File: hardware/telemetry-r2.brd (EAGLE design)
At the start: 65 x 56 mm, 96 parts, among them IC1 RA02, IC10 TPS70933, IC2 TPS70933, IC3 BME280, IC4 STM32L052C8T6, IC5 TPS62160, IC6 HX1, IC7 LMP7702, IC8 ADXL345, IC9 VN5160S-E, J1 GPS1, J2 RASPBERRYPI-GPIO, J3 POWER, J4 GPS2, J5 DNP, J6 SMA_EDGE, Y1 32768, Y2 8M

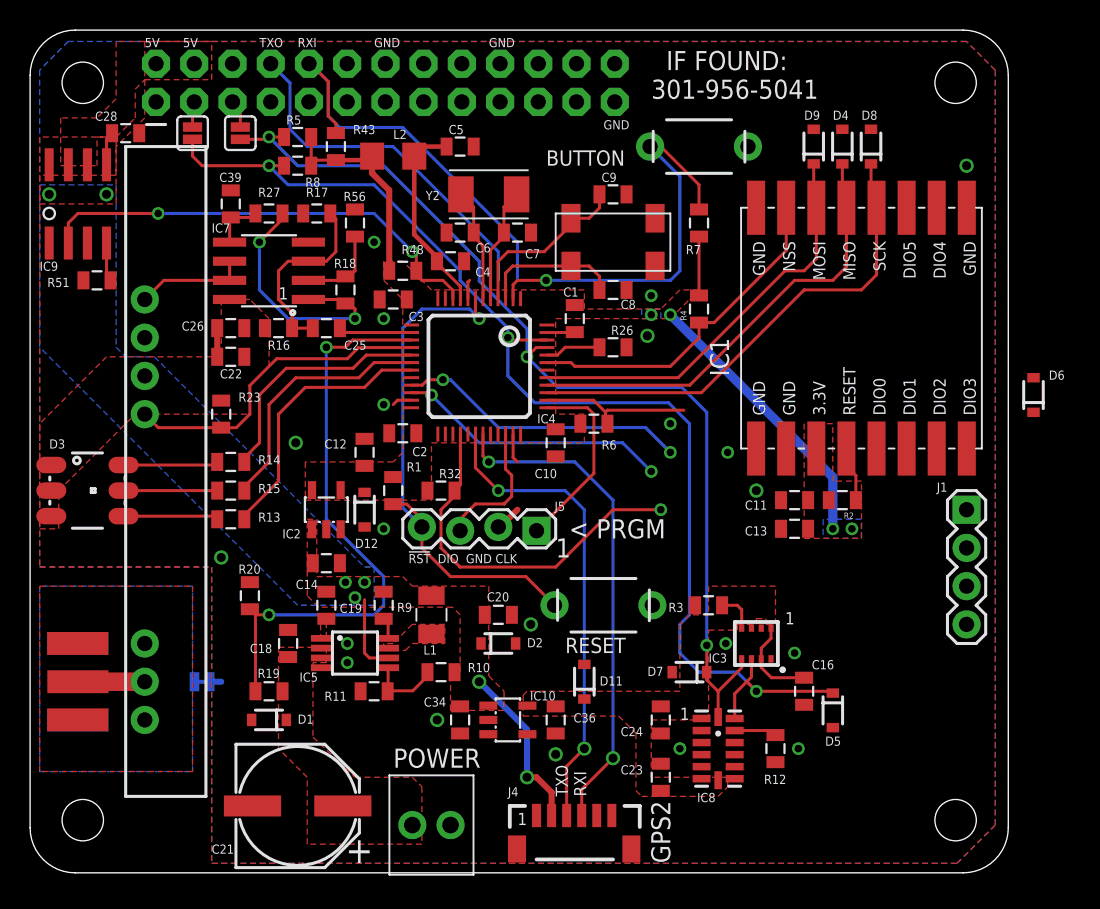
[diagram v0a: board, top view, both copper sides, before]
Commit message: Initial route for HAB v3 modular base board
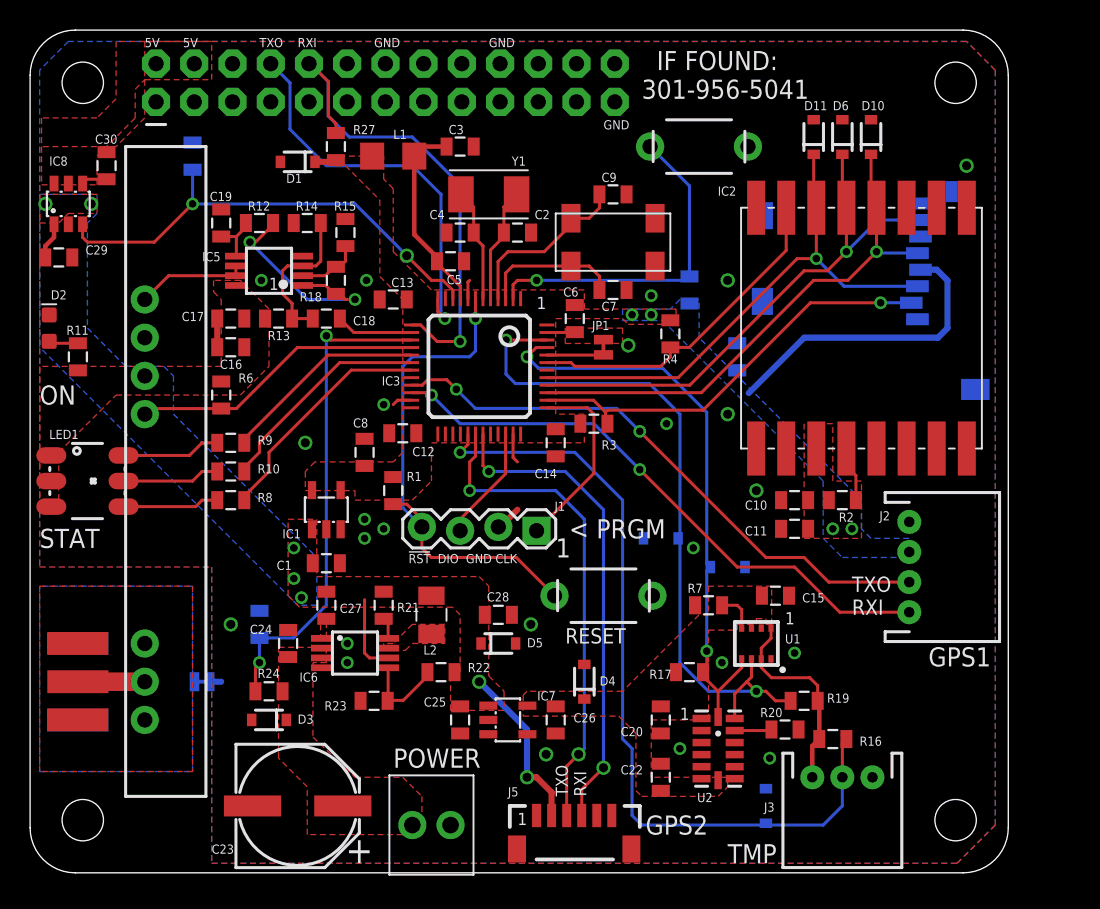
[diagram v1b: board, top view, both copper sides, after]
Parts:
- removed C34: 0.1u, SparkFun-Passives:0805
- removed C36: 1u, SparkFun-Passives:0805
- removed C39: 100p, SparkFun-Passives:0805
- removed D12: 5.6V, SparkFun-DiscreteSemi:SOD-323
- removed IC10: TPS70933, texas:SOT23-DBV
- removed IC9: VN5160S-E, HAB:SO8
- removed JP3: SDA, SparkFun-Jumpers:SMT-JUMPER_2_NO_SILK
- removed JP4: SCL, SparkFun-Jumpers:SMT-JUMPER_2_NO_SILK
- removed R32: 4.7K, SparkFun-Passives:0805
- removed R43, R48, R51: 10K, SparkFun-Passives:0805
- removed R56: 430K, SparkFun-Passives:0805
- added C15, C17, C29: 0.1u, SparkFun-Passives:0805
- added C27: 10u, SparkFun-Passives:0805
- added C30: 1n, SparkFun-Passives:0805
- added D10: 5.6V, SparkFun-DiscreteSemi:SOD-323
- added J$1: SMA_EDGE, SparkFun-Connectors:SMA-EDGE
- added J7: RASPBERRYPI-GPIO, HAB:2X13-PI
- added JP1: (no value), SparkFun-Jumpers:SMT-JUMPER_2_NC_TRACE_NO-SILK
- added LED1: COM-10866, SparkFun-LED:LED-TRICOLOR-5050
- added R21: 10K, SparkFun-Passives:0805
- added R22, R24: 430K, SparkFun-Passives:0805
- added R25: 100K, SparkFun-Passives:0805
- added U1: BME280, BME280ComponentLibrary:BME280_LGA
- added U2: ADXL345, SparkFun-Sensors:LGA14
- C11, C28: value 0.1u -> 10u
- C12, C22, C5: value 1u -> 0.1u
- C13: value 10u -> 0.1u
- C16, C26, C3: value 0.1u -> 1u
- C18: value 1u -> 330p
- C19: value 10u -> 100p
- C2, C4: value 0.1u -> 33p
- C20: value 10u -> 1.0u
- C21: value 100u -> 1u; device SparkFun-Passives:PANASONIC_E -> SparkFun-Passives:0805
- C23: value 0.1u -> 100u; device SparkFun-Passives:0805 -> SparkFun-Passives:PANASONIC_E
- C24: value 1.0u -> 1u
- C25: value 330p -> 0.1u
- C6: value 33p -> 0.1u
- C7: value 33p -> 10p
- C8: value 10p -> 1u
- D1: value 15V -> 5.6V
- D2: value 5.6V -> GREEN; device SparkFun-DiscreteSemi:SOD-323 -> SparkFun-LED:LED-0603
- D3: value COM-10866 -> 15V; device SparkFun-LED:LED-TRICOLOR-5050 -> SparkFun-DiscreteSemi:SOD-323
- IC1: value RA02 -> TPS70933; device HAB:RA02 -> texas:SOT23-DBV
- IC2: value TPS70933 -> RA02; device texas:SOT23-DBV -> HAB:RA02
- IC3: value BME280 -> STM32L052C8T6; device BME280ComponentLibrary:BME280_LGA -> stm32xx:TQFP48
- IC4: value STM32L052C8T6 -> HX1; device stm32xx:TQFP48 -> HAB:HX1
- IC5: value TPS62160 -> LMP7702; device HAB:MSOP8 -> HAB:VSSOP8
- IC6: value HX1 -> TPS62160; device HAB:HX1 -> HAB:MSOP8
- IC7: value LMP7702 -> TPS70933; device SparkFun-AnalogIC:SO08 -> texas:SOT23-DBV
- IC8: value ADXL345 -> TPS22918; device SparkFun-Sensors:LGA14 -> HAB:SOT23-6L
- J1: value GPS1 -> DNP; device SparkFun-Connectors:1X04 -> SparkFun-Connectors:1X04_LOCK@1
- J2: value RASPBERRYPI-GPIO -> GPS1; device HAB:2X13-PI -> SparkFun-Connectors:JST-4-PTH
- J3: value POWER -> TEMP; device HAB:1X02_SCREW -> SparkFun-Connectors:JST-3-PTH
- J4: value GPS2 -> POWER; device SparkFun-Connectors:1X06-1MM -> HAB:1X02_SCREW
- J5: value DNP -> GPS2; device SparkFun-Connectors:1X04_LOCK -> SparkFun-Connectors:1X06-1MM
- J6: value SMA_EDGE -> MICRO-SD_CARD_SOCKET; device SparkFun-Connectors:SMA-EDGE -> SparkFun-Connectors:MICRO-SD-SOCKET
- L1: value 2.2u -> FERRITE; device HAB:1008 -> HAB:1206
- L2: value FERRITE -> 2.2u; device HAB:1206 -> HAB:1008
- R10: value 430K -> 560
- R11: value 82K -> 3.3K
- R12: value 10K -> 330K
- R13: value 220 -> 820K
- R14: value 220 -> 220K
- R15: value 330 -> 430K
- R16: value 820K -> 4.7K
- R17: value 220K -> 3.3K
- R19: value 430K -> 3.3K
- R20: value 100K -> 10K
- R23: value 4.7K -> 82K
- R27: value 330K -> 10K
- R5: value 3.3K -> 10K
- R6: value 10K -> 4.7K
- R8: value 3.3K -> 470
- R9: value 10K -> 470
- Y1: value 32768 -> 8M; device HAB:ABS25 -> SparkFun-FreqCtrl:CRYSTAL-TXC-7A
- Y2: value 8M -> 32768; device SparkFun-FreqCtrl:CRYSTAL-TXC-7A -> HAB:ABS25
- moved J6 57.4 mm to (48.3, 45.7), flipped to the bottom
- moved IC8 56.3 mm to (2.54, 44.5), turned to 0 degrees
- moved R12 48.9 mm to (15.2, 43.2), turned to 180 degrees
- moved J2 47.4 mm to (58.4, 20.3), turned to 270 degrees
- moved R16 45.8 mm to (53.3, 8.89)
- moved C16 44.4 mm to (13.3, 34.9), turned to 180 degrees
- moved D8 44.4 mm to (48.9, 4.45), flipped to the bottom
- moved C21 41.8 mm to (47.0, 34.3), flipped to the bottom, turned to 90 degrees
- moved C28 40.5 mm to (31.1, 17.1)
- moved C22 40.0 mm to (41.9, 6.35), turned to 90 degrees
- moved D4 39.5 mm to (36.8, 12.7)
- moved D11 39.3 mm to (52.1, 48.9)
- moved R17 39.3 mm to (43.8, 13.3), turned to 180 degrees
- moved IC1 37.6 mm to (19.7, 24.1), turned to 0 degrees
- moved IC2 37.6 mm to (55.2, 36.2), turned to 90 degrees
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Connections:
- removed net D_PI: IC9.4, R51.2
- removed net GPSRX: IC4.22, J1.2
- removed net GPSTX: IC4.21, J1.1
- removed net R_SCL: J2.5, JP4.1
- removed net R_SDA: J2.3, JP3.1
- new net CT: C30.1, IC8.4
- new net GPSRX1: IC3.22, J2.4
- new net GPSTX1: IC3.21, J2.3
- new net PLED: D2.A, R11.2
- net !LORA_IRQ!: now also IC2.5; no longer IC1.5
- net !LORA_RST!: now also IC2.4; no longer IC1.4
- net !RST!: now also IC3.7, J1.4; no longer IC4.7, J5.4
- net 3.3V: now also C14.1, C21.1, C6.1, C8.1, D1.C, IC1.5, IC2.3, IC3.1, IC3.24, IC3.36, IC3.48, J2.2, J6.VCC, L1.1, R27.2, R3.2; no longer C1.1, C2.1, C3.1, D12.C, IC1.3, IC2.5, IC4.1, IC4.24, IC4.36, IC4.48, J1.4, L2.1, R32.2, R43.2, R48.2, R6.2, R7.2, R8.2
- net 3V_PI: now also J7.1; no longer J2.1
- net 3V_PI2: now also J7.17; no longer J2.17
- net 5V: now also C1.1, C16.1, C17.1, C25.1, C27.1, C29.1, D5.C, IC1.1, IC4.5, IC5.8, IC6.6, IC7.1, IC8.1, J5.2, L2.2, LED1.1, LED1.2, LED1.3, R11.1, R13.2, R21.2, R22.2, R6.2; no longer C14.1, C19.1, C20.1, C22.1, C26.1, C34.1, D2.C, D3.1, D3.2, D3.3, IC10.1, IC2.1, IC5.6, IC6.5, IC7.8, IC9.5, IC9.8, J4.2, L1.2, R10.2, R16.2, R23.2, R9.2
- net 5V_PI: now also IC8.6, J7.2, J7.4; no longer IC9.6, IC9.7, J2.2, J2.4
- net A+: now also C18.2, IC5.3, R13.1, R14.2; no longer C25.2, IC7.3, R16.1, R17.2
- net A-: now also IC5.2, R15.2; no longer IC7.2, R56.2
- net ADXL_SDO: now also R20.2, U2.12; no longer IC8.12, R12.2
- net BC: now also LED1.4, R8.2; no longer D3.4, R13.2
- net BME_SDO: now also R7.2, U1.P$5; no longer IC3.P$5, R3.2
- net BOOT0: now also IC3.44, JP1.1; no longer IC4.44, R26.1
- net BTN: now also IC3.2, R5.1; no longer IC4.2, R7.1
- net DAC: now also C18.1, IC3.14; no longer C25.1, IC4.14
- net FB5: now also IC6.5, R22.1, R23.2; no longer IC5.5, R10.1, R11.2
- net GC: now also LED1.6, R9.2; no longer D3.6, R14.2
- net GND: now also C15.2, C17.2, C21.2, C23.-, C25.2, C27.2, C29.2, C30.2, D10.A, D2.C, D3.A, IC1.4, IC2.1, IC2.16, IC2.9, IC3.23, IC3.35, IC3.47, IC3.8, IC4.6, IC6.1, IC6.4, IC7.2, J1.2, J2.1, J3.1, J4.2, J5.1, J5.5, J6.GND, J6.GND1, J6.GND3, J7.14, J7.20, J7.25, J7.6, J7.9, JP1.2, R14.1, R15.1, R23.1, R25.1, R7.1, U1.P$1, U1.P$7, U2.2, U2.4, U2.5; no longer C18.2, C21.-, C23.2, C34.2, C36.2, C39.2, D12.A, D2.A, IC1.1, IC1.16, IC1.9, IC10.2, IC2.4, IC3.P$1, IC3.P$7, IC4.23, IC4.35, IC4.47, IC4.8, IC5.1, IC6.6, IC7.4, IC8.4, IC8.5, IC9.1, J1.3, J2.14, J2.20, J2.25, J2.6, J2.9, J3.2, J4.1, J4.5, J5.2, R11.1, R12.1, R17.1, R3.1, R51.1, R56.1
- net GPSRX2: now also IC3.31, J5.4; no longer IC4.31, J4.4
- net GPSTX2: now also IC3.30, J5.3; no longer IC4.30, J4.3
- net HXEN: now also IC3.16, IC4.4, R6.1; no longer IC4.16, IC6.4, R23.1
- net INT: now also U2.8; no longer IC8.8
- net INT2: now also U2.9; no longer IC8.9
- net K_PI: now also IC3.10, IC8.3, R26.1; no longer IC4.10, IC9.2, R48.1
- net LCS: now also IC2.15, IC3.43; no longer IC1.15, IC4.43
- net LEDB: now also IC3.19, R8.1; no longer IC4.19, R13.1
- net LEDG: now also IC3.17, R9.1; no longer IC4.17, R14.1
- net LEDR: now also IC3.18, R10.1; no longer IC4.18, R15.1
- net LP1: now also IC5.1, R12.1; no longer IC7.1, R27.1
- net LP2: now also C19.1, IC5.5, R12.2; no longer C39.1, IC7.5, R27.2
- net MISO: now also D6.C, IC2.13, IC3.40, J6.DO; no longer D4.C, IC1.13, IC4.40
- net MOSI: now also D11.C, IC2.14, IC3.41, J6.DI; no longer D9.C, IC1.14, IC4.41
- net OSC32_IN: now also C7.1, IC3.3, Y2.1; no longer C8.1, IC4.3, Y1.1
- net OSC32_OUT: now also IC3.4, Y2.4; no longer IC4.4, Y1.4
- net OSC_IN: now also C2.1, IC3.5, Y1.P$1; no longer C7.1, IC4.5, Y2.P$1
- net OSC_OUT: now also C4.1, IC3.6, Y1.P$2; no longer C6.1, IC4.6, Y2.P$2
- net PG5: now also IC6.8, R21.1; no longer IC5.8, R9.1
- net RC: now also LED1.5, R10.2; no longer D3.5, R15.2
- net RF_HX1: now also IC4.2, J$1.SIG; no longer IC6.2, J6.SIG
- net RGND: now also IC4.1, IC4.3, J$1.GND@0, J$1.GND@1, J$1.GND@2, J$1.GND@3; no longer IC6.1, IC6.3, J6.GND@0, J6.GND@1, J6.GND@2, J6.GND@3
- net R_CS0: now also J7.24; no longer J2.24
- net R_CS1: now also J7.26; no longer J2.26
- net R_MISO: now also J7.21; no longer J2.21
- net R_MOSI: now also J7.19; no longer J2.19
- net R_RX: now also IC3.13, J7.10, R27.1; no longer IC4.13, J2.10, R43.1
- net R_SCK: now also J7.23; no longer J2.23
- net R_TX: now also IC3.12, J7.8; no longer IC4.12, J2.8
- net SCK: now also D10.C, IC2.12, IC3.39, J6.SCLK; no longer D8.C, IC1.12, IC4.39
- net SCL: now also D9.C, IC3.45, R17.1, U1.P$4, U2.14; no longer D7.C, IC3.P$4, IC4.45, IC8.14, JP4.2, R5.1
- net SDA: now also D7.C, IC3.46, R19.1, U1.P$3, U2.13; no longer D5.C, IC3.P$3, IC4.46, IC8.13, JP3.2, R8.1
- net SDCS: now also IC3.38, J6.CS, R3.1; no longer IC4.38, R6.1
- net SW5: now also IC6.7, L2.1; no longer IC5.7, L1.1
- net SWCLK: now also IC3.37, J1.1; no longer IC4.37, J5.1
- net SWDIO: now also IC3.34, J1.3; no longer IC4.34, J5.3
- net TEMP: now also D8.C, IC3.29, J3.2, R16.1; no longer D6.C, IC4.28, R32.1
- net TXD: now also IC4.7, IC5.6, IC5.7; no longer IC6.7, IC7.6, IC7.7
- net U_RX: now also IC3.42; no longer IC4.42
- net VBAT: now also C23.+, C24.1, D3.C, IC6.2, IC6.3, J4.1, R24.2; no longer C18.1, C21.+, D1.C, IC5.2, IC5.3, J3.1, R19.2
- net VDDA: now also C3.1, IC3.9, L1.2; no longer C4.1, IC4.9, L2.2
- net VDIV: now also IC3.15, R24.1, R25.2; no longer IC4.15, R19.1, R20.2
- net VS: now also C15.1, C20.1, C22.1, C26.1, D4.C, IC7.5, J3.3, R16.2, R17.2, R19.2, U1.P$2, U1.P$6, U1.P$8, U2.1, U2.6, U2.7; no longer C16.1, C23.1, C24.1, C36.1, D11.C, IC10.5, IC3.P$2, IC3.P$6, IC3.P$8, IC8.1, IC8.6, IC8.7
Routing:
- net GPSRX1: track 0.00 -> 39.1 mm, vias 0 -> 2
- net GPSTX1: track 0.00 -> 38.8 mm, vias 0 -> 2
- net SDA: track 79.5 -> 48.0 mm, vias 3 -> 2
- net TEMP: track 24.8 -> 54.5 mm
- net SCL: track 66.4 -> 38.8 mm, vias 3 -> 2
- net GPSTX: track 19.3 -> 0.00 mm, vias 2 -> 0
- net GPSRX: track 18.1 -> 0.00 mm, vias 2 -> 0
- net SDCS: track 10.3 -> 28.4 mm, vias 0 -> 1
- net 3.3V: track 36.9 -> 21.7 mm
- net MOSI: track 27.5 -> 35.7 mm, vias 0 -> 1
- net VS: track 6.02 -> 13.5 mm
- net VDIV: track 39.0 -> 32.7 mm
- net R_RX: track 28.1 -> 34.2 mm, vias 0 -> 1
- net MISO: track 30.1 -> 35.7 mm, vias 0 -> 1
- net BTN: track 27.4 -> 22.6 mm
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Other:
- board text added: "GPS1"
- board text added: "ON"
- board text added: "STAT"
- board text added: "TMP"
- board text removed: "BUTTON"
